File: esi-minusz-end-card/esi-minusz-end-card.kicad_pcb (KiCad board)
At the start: 4 copper layers, 99.8 x 94.6 mm, 93 parts, among them J1 J-SAMTEC-TFM-120-01-L-D-RA, J2 U.FL-R-SMT-1, J3 M55-7101242R, J5 M55-7101242R, J6 +UHF, J7 -UHF, Q1 DMP2240UDM, Q2 PMV45EN, Q3 PMV45EN, Q4 PMV45EN, Q5 DMP2240UDM-7, Q6 PMV45EN, Q7 DMP2240UDM-7, U1 NCS2-62+, U11 MIC842LYC5, U12 MIC842LYC5, U2 MAX7310, U201 TS5A21366, U202 TS5A21366, U203 TS5A21366, U204 TS5A21366

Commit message: renamed ESI -Z end card to combat Shae's weird naming conventions
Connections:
- net /+UHF renamed Net-(J6-Pad1)
- net /-UHF renamed Net-(J7-Pad1)

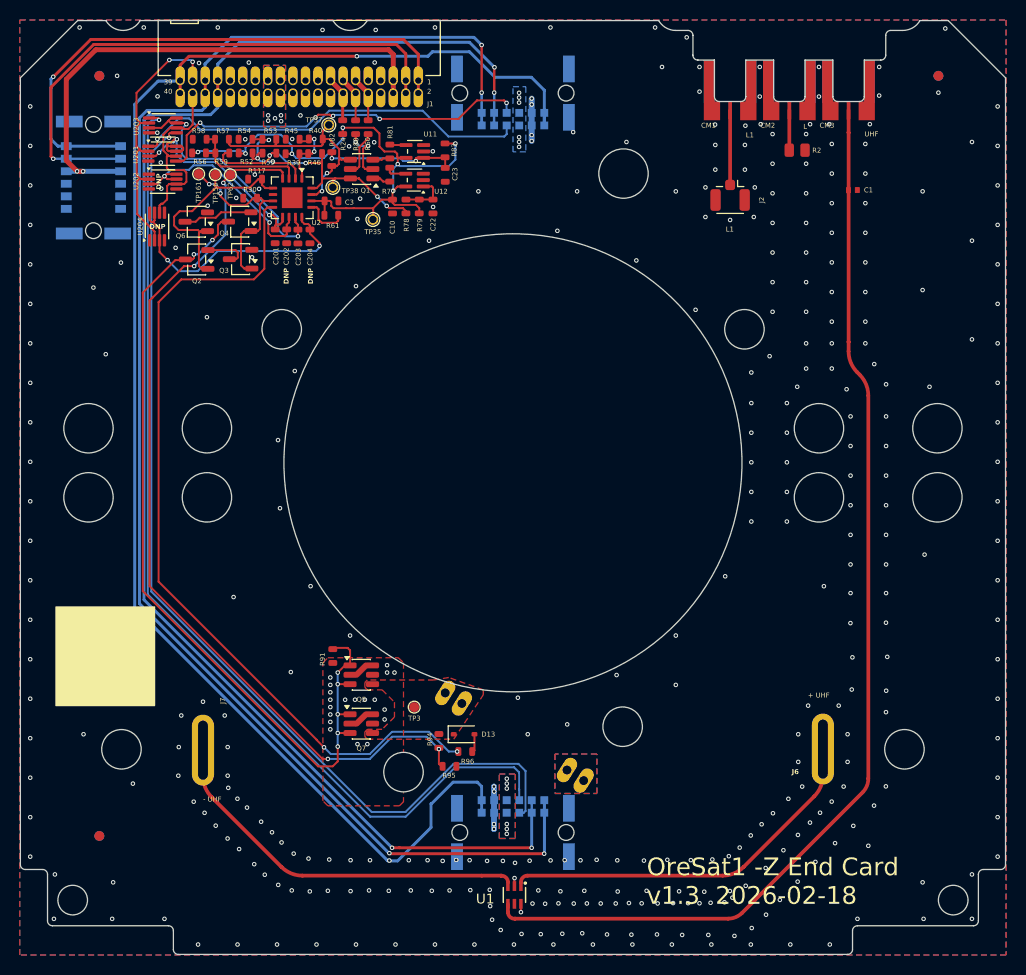
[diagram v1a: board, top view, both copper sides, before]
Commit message: Finalized dipole changes, added -/+ Y solar mods. Believe this is finished
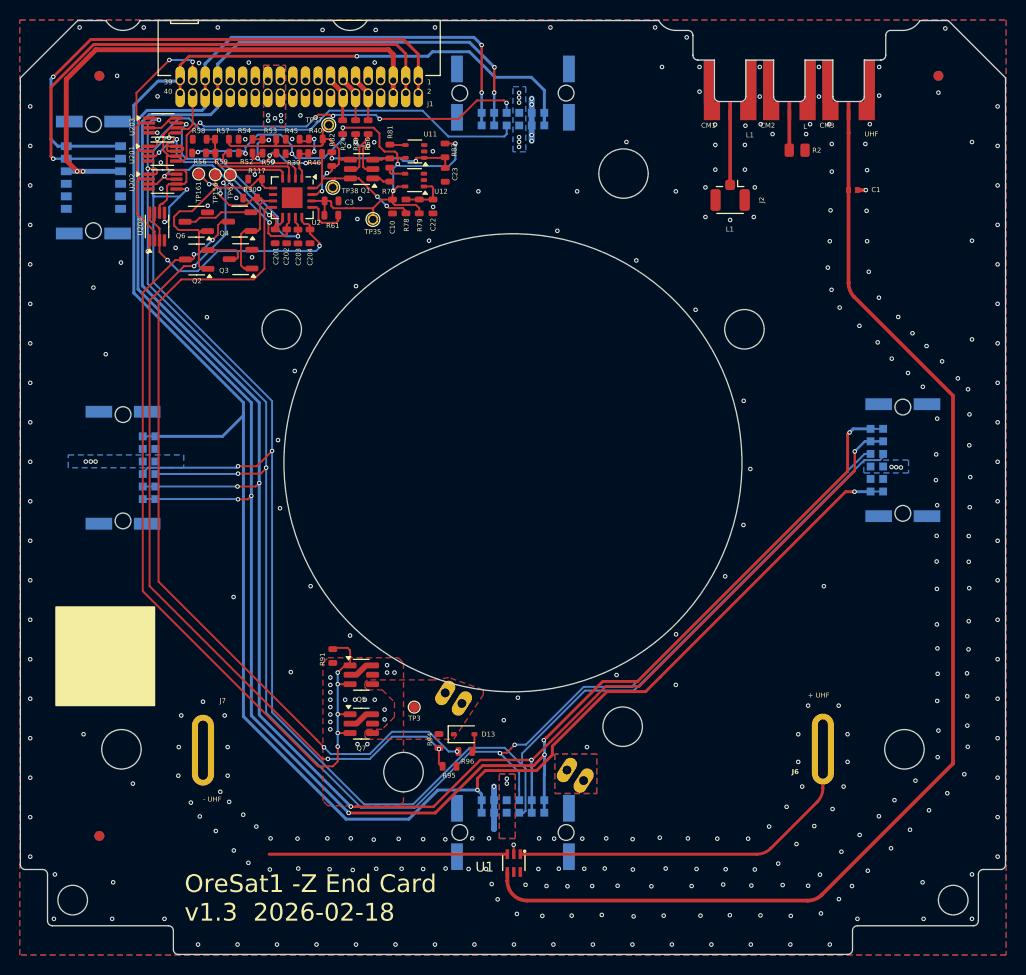
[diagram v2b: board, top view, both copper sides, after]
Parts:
- removed H101, H102, H103, H104, H105, H106, H107, H108: MountingHole, MountingHole:MountingHole_5mm
- added J4: M55-7101242R, oresat-connectors:J-Harwin-M55-7101242R, B.Cu at (188.0, 102.2)
- added J8: M55-7101242R, oresat-connectors:J-Harwin-M55-7101242R, B.Cu at (109.0, 103.0)
- moved U1 3.23 mm to (148.6, 143.1)
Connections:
- net Net-(J6-Pad1) renamed /+UHF
- net Net-(J7-Pad1) renamed /-UHF
- U202 pad 1: /OPD/PY-UART-RX -> /MX_UART_RX
- U202 pad 5: /OPD/PY-UART-TX -> /MX_UART_TX
- U204 pad 1: /OPD/MY-UART-RX -> /MX_UART_RX
- U204 pad 5: /OPD/MY-UART-TX -> /MX_UART_TX
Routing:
- net /MX_UART_TX: track 102.3 -> 176.8 mm, vias 1 -> 5
- net /MX_UART_RX: track 102.1 -> 167.7 mm, vias 1 -> 7
- net /CAN1_L: track 155.4 -> 219.1 mm, vias 4 -> 8
- net /CAN1_H: track 151.4 -> 214.7 mm, vias 4 -> 7
- net /~{SD}: track 157.0 -> 217.7 mm, vias 1 -> 3
- net /UHF: track 111.0 -> 123.2 mm
- net GND: track 10.3 -> 10.4 mm, vias 369 -> 328
- net VBUS: vias 36 -> 38
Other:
- board text removed: "DNP"

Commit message: shifted and softened microstrip curves
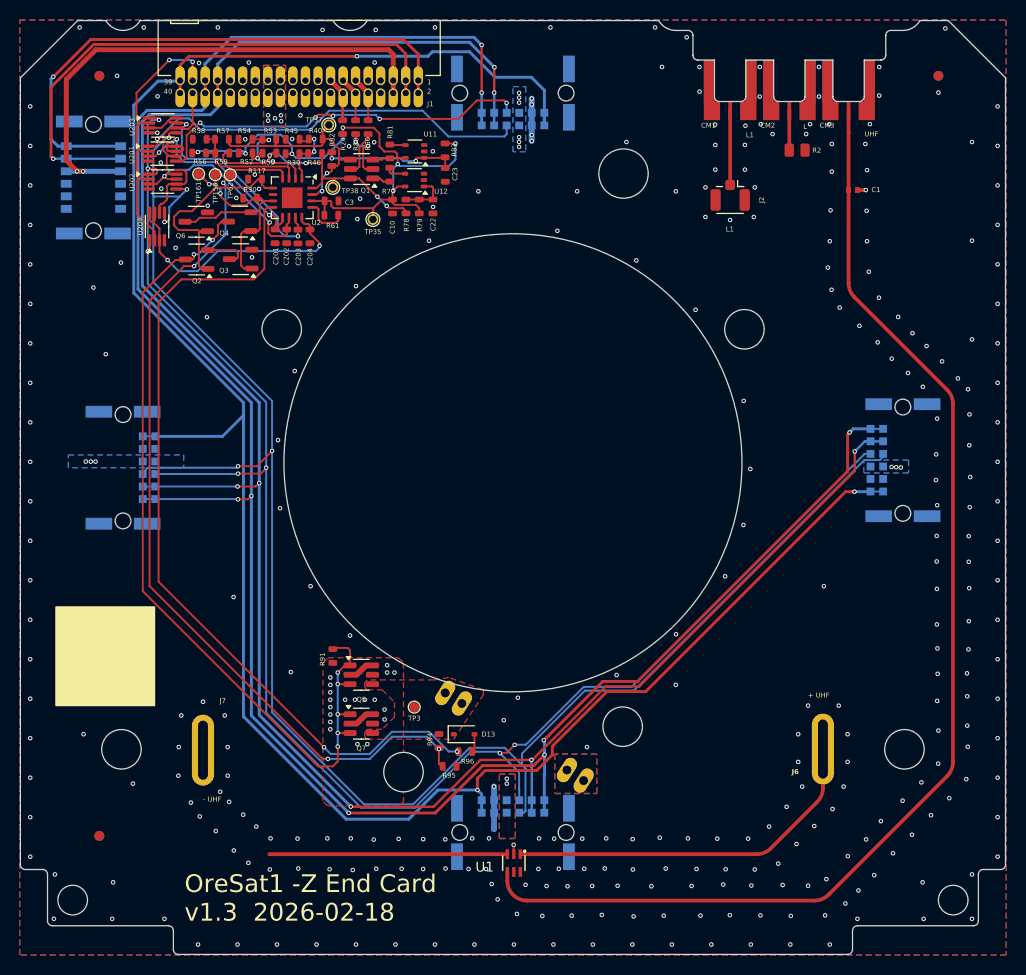
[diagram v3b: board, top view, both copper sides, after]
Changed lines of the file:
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@@
 	(gr_line
 		(start 150.1 146.875)
-		(end 178.675 146.85)
+		(end 180.025 146.85)
 		(stroke
 			(width 2.3)
@@
 	)
 	(gr_line
-		(start 178.675 146.85)
-		(end 179.3 146.625)
-		(stroke
-			(width 2.3)
-			(type default)
-		)
-		(layer "F.Mask")
-	)
-	(gr_line
 		(start 191.025 93.675)
 		(end 182.775 85.35)
@@
 	)
 	(gr_line
-		(start 179.3 146.625)
-		(end 179.9 146.175)
-		(stroke
-			(width 2.3)
-			(type default)
-		)
-		(layer "F.Mask")
-	)
-	(gr_line
-		(start 193 133.025)
+		(start 193.025 133.75)
 		(end 193 95.65)
 		(stroke
@@
 		(layer "F.Mask")
 	)
-	(gr_line
-		(start 191.825 134.325)
-		(end 192.975 133.1)
-		(stroke
-			(width 2.3)
-			(type default)
-		)
-		(layer "F.Mask")
-	)
 	(gr_rect
 		(start 175.4 68.04)
@@
 	)
 	(gr_line
+		(start 192.9625 133.75)
+		(end 180.0375 146.6)
+		(stroke
+			(width 2.3)
+			(type default)
+		)
+		(layer "F.Mask")
+	)
+	(gr_line
 		(start 146.375 142.15)
 		(end 123.488289 142.125)
@@
 		(layer "F.Mask")
 	)
-	(gr_line
-		(start 179.9 146.175)
-		(end 191.875 134.275)
-		(stroke
-			(width 2.3)
-			(type default)
-		)
-		(layer "F.Mask")
-	)
 	(gr_rect
 		(start 102.2 117.1)
@@
 	)
 	(via
-		(at 181.525 146.7)
+		(at 182.175 147.15)
 		(size 0.4572)
 		(drill 0.254)
@@
 	)
 	(via
-		(at 184.45 143.825)
+		(at 185.1 144.275)
 		(size 0.4572)
 		(drill 0.254)
@@
 	)
 	(via
-		(at 185.575 138.3)
+		(at 185.775 138.8)
 		(size 0.4572)
 		(drill 0.254)
@@
 	)
 	(via
-		(at 181.775 141.9)
+		(at 182.425 142.35)
 		(size 0.4572)
 		(drill 0.254)
@@
 	)
 	(via
-		(at 179.7 148.15)
+		(at 180.125 148.35)
 		(size 0.4572)
 		(drill 0.254)
@@
 	)
 	(via
-		(at 187.15 136.675)
+		(at 187.975 136.725)
 		(size 0.4572)
 		(drill 0.254)
@@
 	)
 	(via
-		(at 190.65 137.7)
+		(at 190.85 138.2)
 		(size 0.4572)
 		(drill 0.254)
@@
 	)
 	(via
-		(at 189.275 134.7)
+		(at 189.875 134.875)
 		(size 0.4572)
 		(drill 0.254)
@@
 	)
 	(via
-		(at 188.725 139.675)
+		(at 188.925 140.175)
 		(size 0.4572)
 		(drill 0.254)
@@
 	)
 	(via
-		(at 179.6 144.225)
+		(at 180.25 144.675)
 		(size 0.4572)
 		(drill 0.254)
@@
 	)
 	(via
-		(at 186.8 141.55)
+		(at 187 142.05)
 		(size 0.4572)
 		(drill 0.254)
@@
 	)
 	(via
-		(at 192.5 135.975)
+		(at 192.7 136.475)
 		(size 0.4572)
 		(drill 0.254)
@@
 	)
 	(via
-		(at 194.225 134.05)
+		(at 194.425 134.55)
 		(size 0.4572)
 		(drill 0.254)
@@
 	)
 	(via
-		(at 182.85 145.375)
+		(at 183.5 145.825)
 		(size 0.4572)
 		(drill 0.254)
@@
 	)
 	(via
-		(at 191.525 132.325)
+		(at 191.575 132.975)
 		(size 0.4572)
 		(drill 0.254)
@@
 	)
 	(via
-		(at 183.625 140.2)
+		(at 184.275 140.65)
 		(size 0.4572)
 		(drill 0.254)
@@
 	)
 	(segment
-		(start 182.5 69.05)
-		(end 182.500002 66.799993)
+		(start 147.93 143.95)
+		(end 147.93 144.85)
 		(width 0.38)
 		(layer "F.Cu")
@@
 	)
 	(segment
-		(start 193.075 95.7)
+		(start 182.500002 69.050002)
+		(end 182.5 69.05)
+		(width 0.38)
+		(layer "F.Cu")
+		(net 7)
+	)
+	(segment
+		(start 192.489213 95.114213)
 		(end 183.083362 85.708362)
 		(width 0.38)
@@
 	)
 	(segment
-		(start 147.93 143.95)
-		(end 147.93 144.85)
+		(start 193.075 132.821573)
+		(end 193.075 96.528427)
 		(width 0.38)
 		(layer "F.Cu")
@@
 	)
 	(segment
-		(start 179.785787 146.264213)
-		(end 193.075 132.975)
+		(start 180.460787 146.264213)
+		(end 192.489214 134.235786)
 		(width 0.38)
 		(layer "F.Cu")
@@
 	)
 	(segment
-		(start 193.075 132.975)
-		(end 193.075 95.7)
+		(start 182.5 69.05)
+		(end 182.500002 66.799993)
 		(width 0.38)
 		(layer "F.Cu")
@@
 	(segment
 		(start 149.93 146.85)
-		(end 178.371573 146.85)
+		(end 179.046573 146.85)
 		(width 0.38)
 		(layer "F.Cu")
 		(net 7)
 	)
-	(segment
-		(start 182.500002 69.050002)
-		(end 182.5 69.05)
+	(arc
+		(start 193.075 132.821573)
+		(mid 192.922759 133.58694)
+		(end 192.489214 134.235786)
+		(width 0.38)
+		(layer "F.Cu")
+		(net 7)
+	)
+	(arc
+		(start 147.93 144.85)
+		(mid 148.515786 146.264214)
+		(end 149.93 146.85)
 		(width 0.38)
 		(layer "F.Cu")
@@
 	)
 	(arc
-		(start 178.371573 146.85)
-		(mid 179.13694 146.697759)
-		(end 179.785787 146.264213)
+		(start 179.046573 146.85)
+		(mid 179.81194 146.697759)
+		(end 180.460787 146.264213)
 		(width 0.38)
 		(layer "F.Cu")
@@
 	)
 	(arc
-		(start 147.93 144.85)
-		(mid 148.515786 146.264214)
-		(end 149.93 146.85)
+		(start 193.075 96.528427)
+		(mid 192.922759 95.76306)
+		(end 192.489213 95.114213)
 		(width 0.38)
 		(layer "F.Cu")
@@
 		(start 174.610787 141.564213)
 		(end 179.314214 136.860786)
-		(width 0.3)
+		(width 0.38)
 		(layer "F.Cu")
 		(net 70)
@@
 		(start 149.25 142.15)
 		(end 173.196573 142.15)
-		(width 0.3)
+		(width 0.38)
 		(layer "F.Cu")
 		(net 70)
@@
 		(start 179.9 135.446573)
 		(end 179.9 131.5)
-		(width 0.3)
+		(width 0.38)
 		(layer "F.Cu")
 		(net 70)
@@
 		(mid 179.747759 136.21194)
 		(end 179.9 135.446573)
-		(width 0.3)
+		(width 0.38)
 		(layer "F.Cu")
 		(net 70)
@@
 		(mid 173.96194 141.997759)
 		(end 173.196573 142.15)
-		(width 0.3)
+		(width 0.38)
 		(layer "F.Cu")
 		(net 70)
@@
 		(start 147.93 142.15)
 		(end 123.803427 142.15)
-		(width 0.3)
+		(width 0.38)
 		(layer "F.Cu")
 		(net 71)
@@
 		(start 117.1 135.446573)
 		(end 117.1 131.61)
-		(width 0.3)
+		(width 0.38)
 		(layers "F.Cu" "F.Mask")
 		(net 71)
@@
 		(start 122.389213 141.564213)
 		(end 117.685786 136.860786)
-		(width 0.3)
+		(width 0.38)
 		(layers "F.Cu" "F.Mask")
 		(net 71)
@@
 		(mid 117.252241 136.21194)
 		(end 117.1 135.446573)
-		(width 0.3)
+		(width 0.38)
 		(layers "F.Cu" "F.Mask")
 		(net 71)
@@
 		(mid 123.03806 141.997759)
 		(end 123.803427 142.15)
-		(width 0.3)
+		(width 0.38)
 		(layers "F.Cu" "F.Mask")
 		(net 71)

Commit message: Fixed OPD connection in schematics and updated tracing and out of date footprints. Ready for final review from andrew
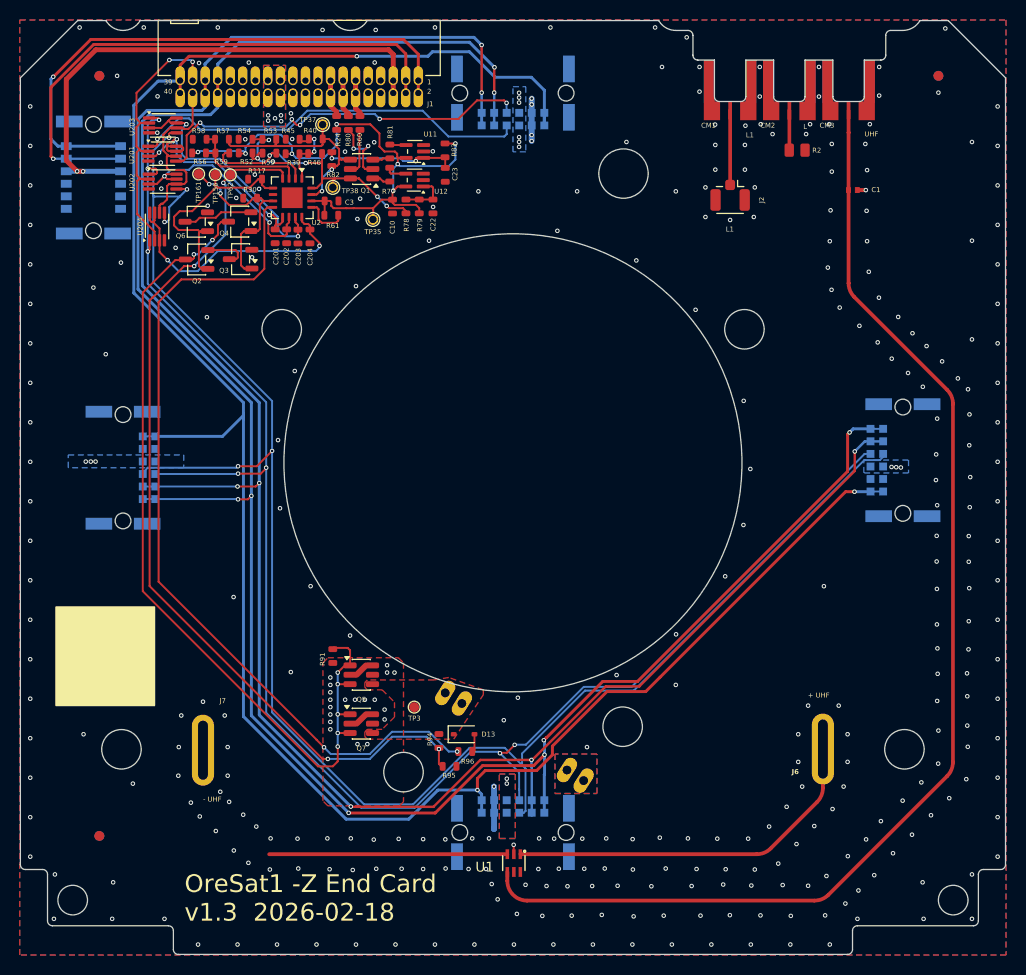
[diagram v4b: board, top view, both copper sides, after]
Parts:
- moved R60 0.94 mm to (133.0, 68.1)
- moved R80 0.84 mm to (131.8, 68.1)
- moved R24 0.75 mm to (130.6, 68.1)
- moved TP37 0.63 mm to (129.2, 68.2)
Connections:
- J1 pad 10: /OPD_SDA -> unconnected-(J1-Pad10)
- J1 pad 12: /OPD_SCL -> /OPD_SDA
- J1 pad 14: /OPD_PWR -> /OPD_SCL
- J1 pad 16: unconnected-(J1-Pad16) -> /OPD_PWR
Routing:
- net Net-(Q1B-S): track 5.79 -> 7.13 mm
- net VPD: track 61.0 -> 61.8 mm
- net /OPD_SDA: track 4.55 -> 3.78 mm
- net /OPD_SCL: track 4.55 -> 3.83 mm
- net /OPD_PWR: track 4.57 -> 3.85 mm
- net /PX_UART_TX: track 39.2 -> 39.8 mm

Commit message: ESI v1.0 -Z End Card for fab
Added makefile and readme, fixed BOM error, moved to better RF zone rules
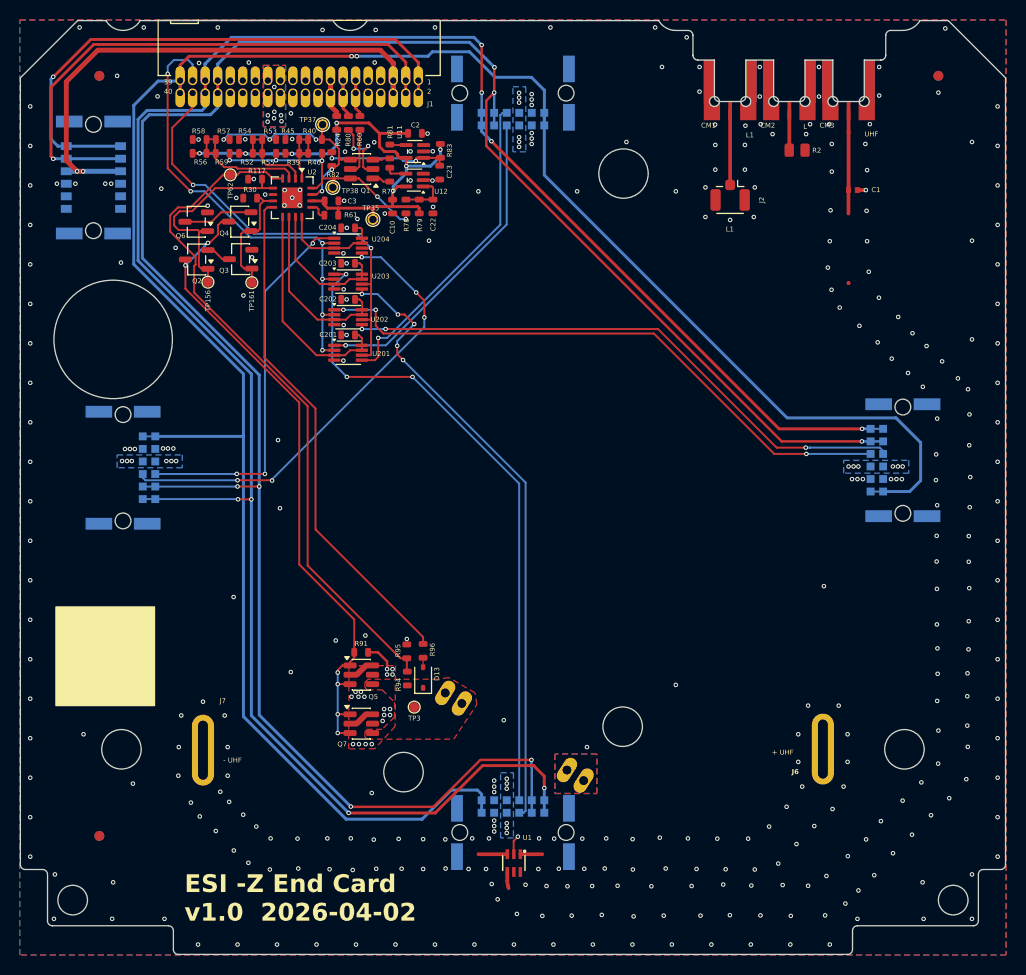
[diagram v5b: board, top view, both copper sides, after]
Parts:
- removed HW5, HW6: M2-Press-Fit-Nut, oresat-misc:M2-Press-Fit-Nut
- added C2: 100n, oresat-passives:0603-C-NOSILK, F.Cu at (138.6, 69.1)
- moved U201 27.6 mm to (131.8, 91.3)
- moved U203 24.5 mm to (131.8, 84.1)
- moved U202 23.3 mm to (131.8, 87.8)
- moved U204 19.5 mm to (131.8, 80.5), turned to 0 degrees
- moved C201 12.4 mm to (131.8, 89.5), turned to 180 degrees
- moved R95 12.4 mm to (137.8, 121.6), turned to 90 degrees
- moved TP161 12.3 mm to (122.0, 84.2)
- moved R96 11.1 mm to (139.4, 121.5), turned to -90 degrees
- moved TP156 10.9 mm to (117.6, 84.2)
- moved C202 8.92 mm to (131.8, 86.0), turned to 180 degrees
- moved D13 7.09 mm to (139.4, 124.2), turned to 90 degrees
- moved R94 7.09 mm to (137.8, 124.3), turned to 90 degrees
- moved C203 5.76 mm to (131.8, 82.3), turned to 180 degrees
- moved C204 3.96 mm to (131.8, 78.7), turned to 180 degrees
- moved R91 2.90 mm to (133.1, 121.7), turned to 180 degrees
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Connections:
- J4 pad 7: /MX_UART_TX -> /PY_UART_TX
- J4 pad 8: /MX_UART_RX -> /PY_UART_RX
- J8 pad 7: /MX_UART_TX -> /MY_UART_TX
- J8 pad 8: /MX_UART_RX -> /MY_UART_RX
- U202 pad 1: /MX_UART_RX -> /PY_UART_RX
- U202 pad 5: /MX_UART_TX -> /PY_UART_TX
- U204 pad 1: /MX_UART_RX -> /MY_UART_RX
- U204 pad 5: /MX_UART_TX -> /MY_UART_TX
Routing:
- net /MX_UART_TX: track 176.8 -> 63.2 mm
- net /MX_UART_RX: track 167.7 -> 66.9 mm, vias 7 -> 3
- net /PY_UART_RX: track 0.00 -> 61.3 mm, vias 0 -> 3
- net /PY_UART_TX: track 0.00 -> 58.7 mm, vias 0 -> 3
- net /MY_UART_TX: track 0.00 -> 46.8 mm, vias 0 -> 5
- net /MY_UART_RX: track 0.00 -> 39.0 mm, vias 0 -> 3
- net /OPD/TEST_ANTENNAS: track 86.6 -> 51.6 mm, vias 2 -> 0
- net /C3-UART-RX: track 19.5 -> 46.3 mm, vias 0 -> 2
- net /OPD/READ_ANTENNAS: track 91.9 -> 70.1 mm, vias 4 -> 0
- net /C3-UART-TX: track 28.3 -> 49.4 mm, vias 2 -> 6
- net Net-(Q2-D): track 87.7 -> 67.2 mm, vias 7 -> 6
- net /OPD/MY_UART_EN: track 27.6 -> 11.0 mm, vias 2 -> 0
- net /OPD/MX_UART_EN: track 26.4 -> 14.4 mm, vias 2 -> 0
- net /~{SD}: track 217.7 -> 226.8 mm, vias 3 -> 2
- net /PX_UART_RX: track 41.1 -> 32.6 mm
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- removed copper zone on In1.Cu, net VBUS

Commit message: ESI -Z End Card updated to v1.1 with extremely minor changes (KiCad 10 update)
Updated to KiCad 10.0.3, which updated several footprints and re-triggered from ERC
and DRCs. Those were fixed, and out of an abundance of caution, we upped the version
number although there's no significant difference with v1.0.
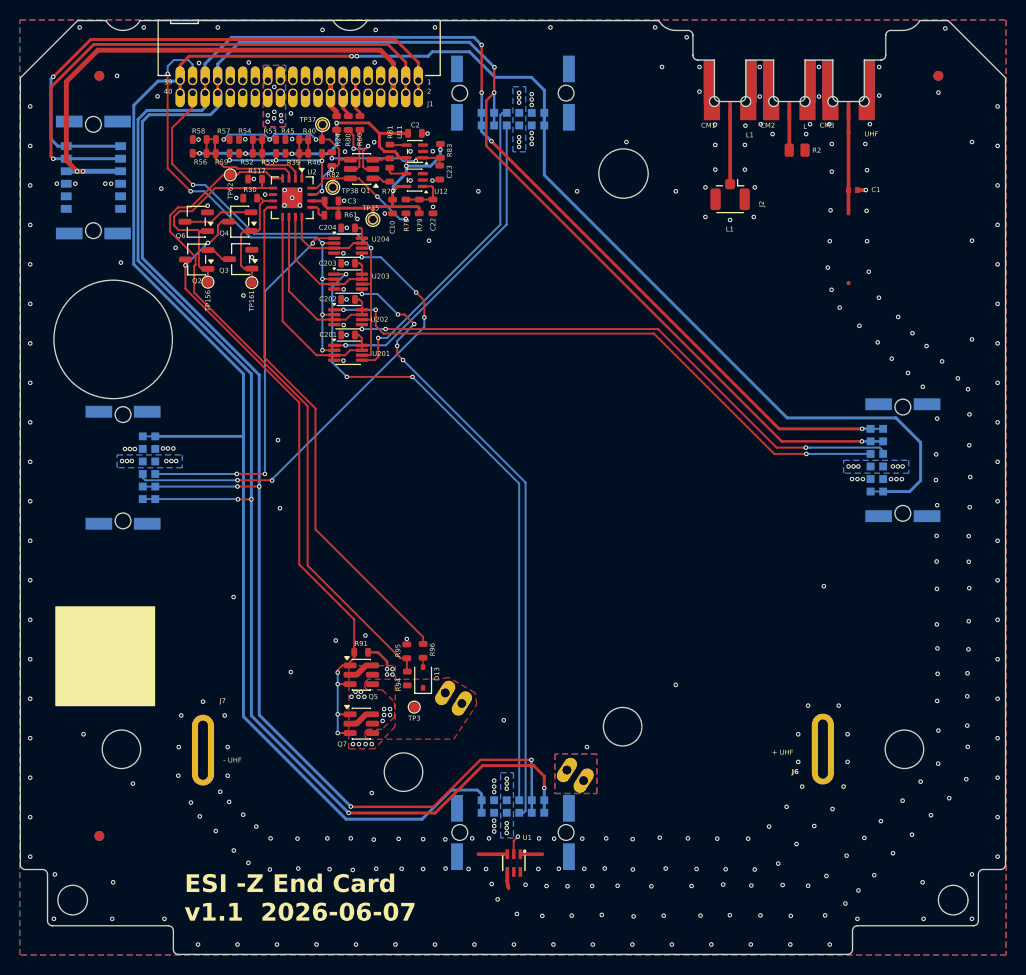
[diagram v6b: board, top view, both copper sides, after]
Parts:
- moved J2 0.40 mm to (170.5, 75.8)
